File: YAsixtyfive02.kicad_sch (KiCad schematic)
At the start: 49 parts, among them J1 ~NMI, J2 Aux 5VDC, J3 Power 5V, J4 Expansion Bus, J5 Port A, J6 Port B, J7 GND, J8 FTDI Serial2USB, SW1 RESET, U1 WD65C02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

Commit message: changed PHI2 out to CLK and PCB tweaks
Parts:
- added JP4: ACIA CLK SEL, Connector_PinHeader_2.54mm:PinHeader_1x03_P2.54mm_Vertical, symbol Connector:Conn_01x03_Male
- U8: footprint 21-0248A -> Package_TO_SOT_THT:TO-92
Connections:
- net CLK: now also J4.20 (Pin_20), U4.5, U7.25 (PHI2), U9.14 (E/ϕ2), JP4.1 (Pin_1); no longer J4.36 (Pin_36), U9.3 (Rx_CLK), U9.4 (Tx_CLK)
- removed net PHI2: J4.20 (Pin_20), U1.39 (PHI2out), U4.5, U7.25 (PHI2), U9.14 (E/ϕ2)
- new net ACIA_CLK: J4.36 (Pin_36), JP4.3 (Pin_3)
- new net TX_CLK: JP4.2 (Pin_2), U9.3 (Rx_CLK), U9.4 (Tx_CLK)
- no-connect marks 13 -> 14

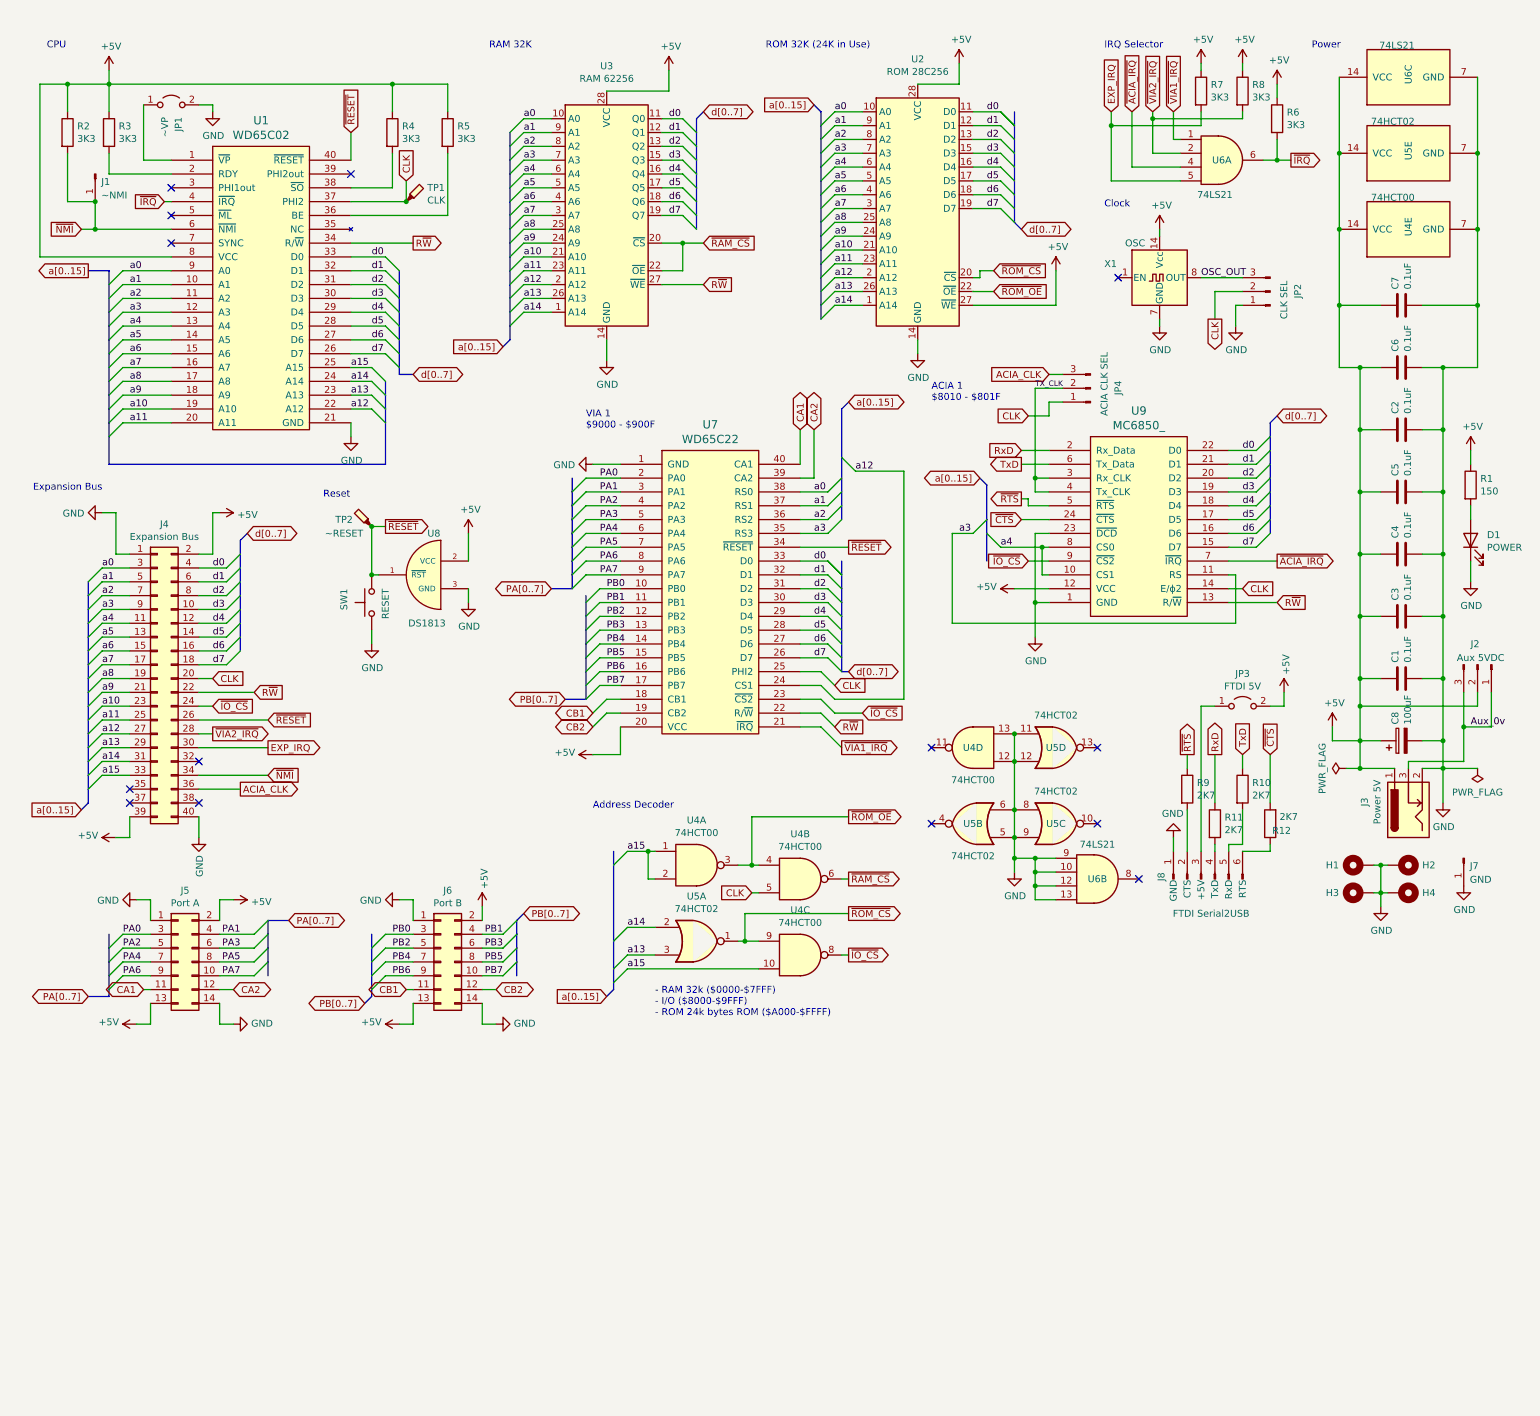
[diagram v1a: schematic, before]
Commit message: Simplified board for backplane  only CPU/RAM/ROM/ACIA/Glue
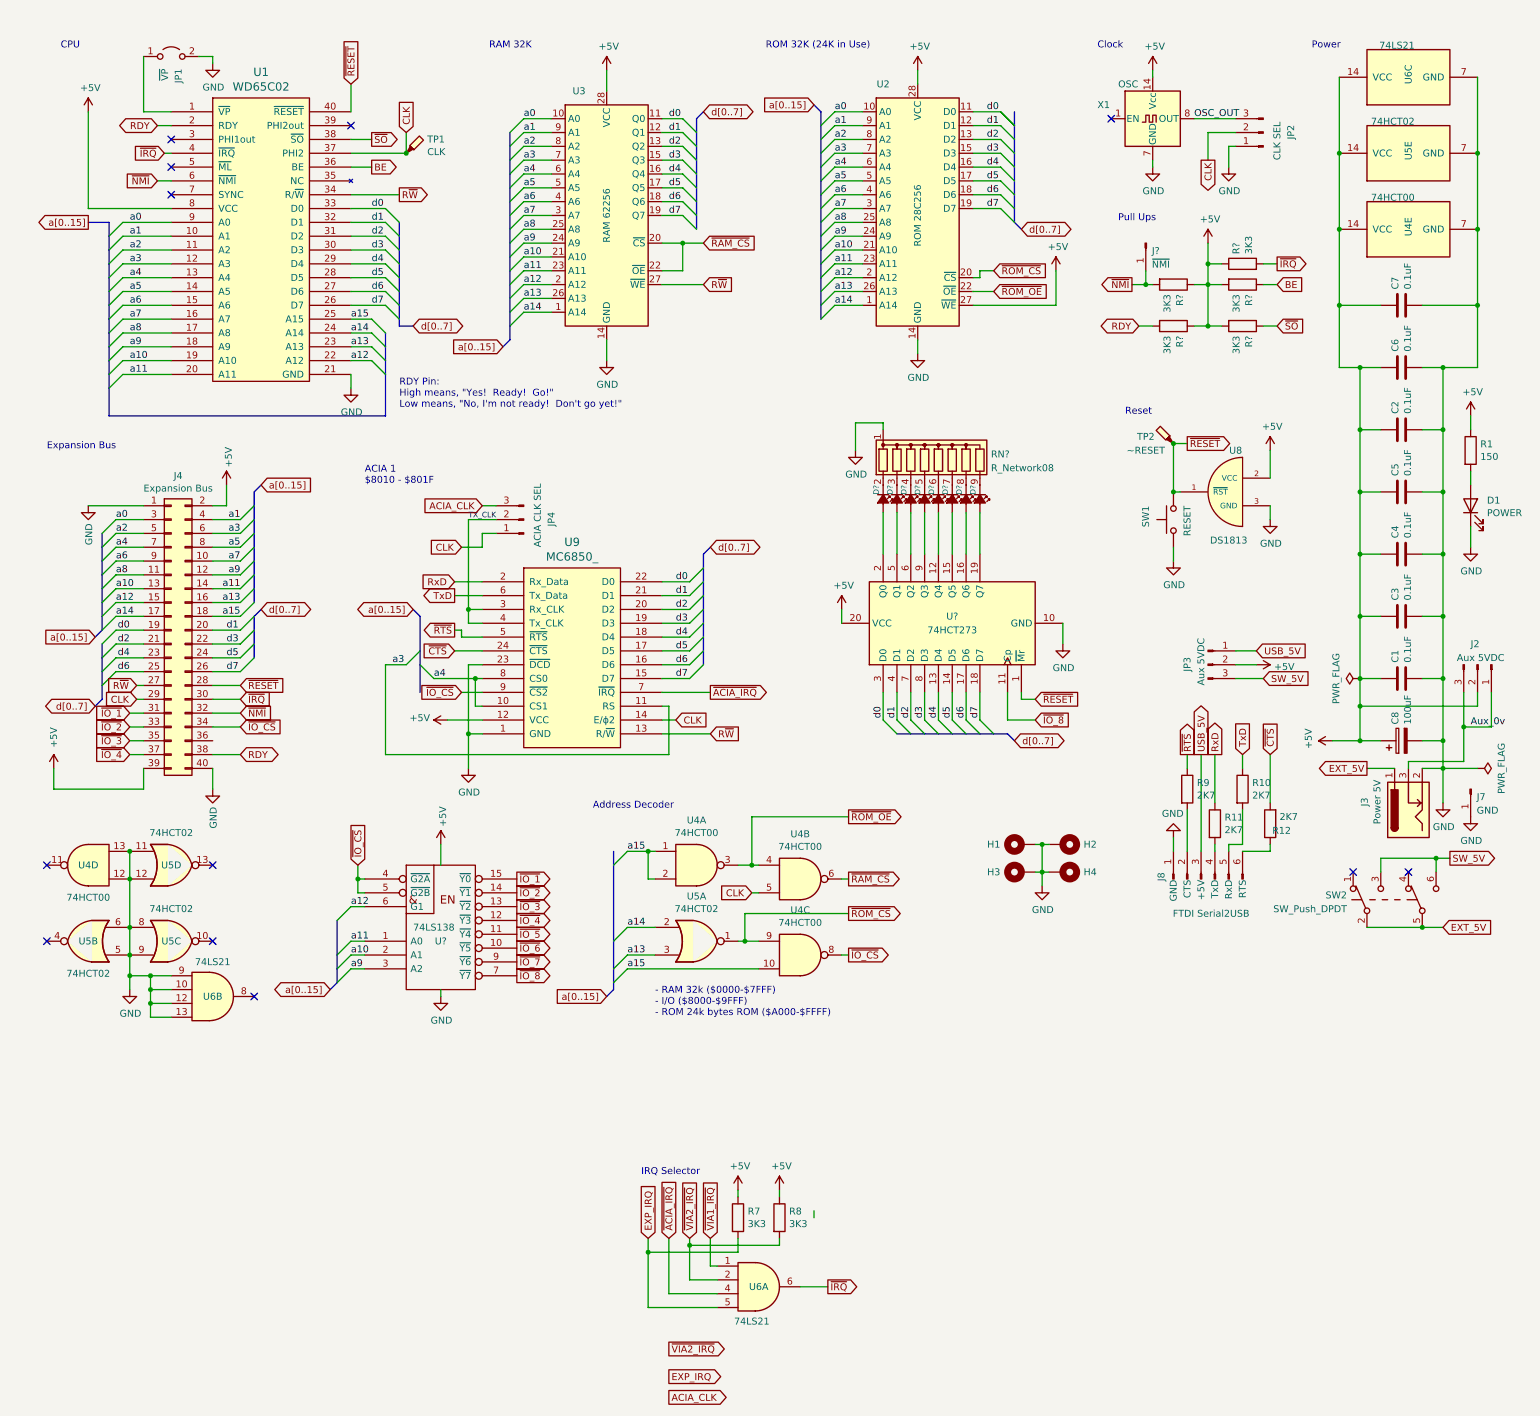
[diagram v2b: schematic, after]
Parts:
- removed J1: ~NMI, Connector_PinHeader_2.54mm:PinHeader_1x01_P2.54mm_Vertical, symbol Connector:Conn_01x01_Male
- removed J5: Port A, Connector_PinSocket_2.54mm:PinSocket_2x07_P2.54mm_Vertical, symbol Connector_Generic:Conn_02x07_Odd_Even
- removed J6: Port B, Connector_PinSocket_2.54mm:PinSocket_2x07_P2.54mm_Vertical, symbol Connector_Generic:Conn_02x07_Odd_Even
- removed JP3: FTDI 5V, Connector_PinHeader_2.54mm:PinHeader_2x01_P2.54mm_Vertical, symbol Jumper:Jumper_2_Open
- removed R2, R3, R4, R5, R6: 3K3, Resistor_THT:R_Axial_DIN0207_L6.3mm_D2.5mm_P10.16mm_Horizontal, symbol Device:R
- removed U7: WD65C22, Package_DIP:DIP-40_W15.24mm_Socket_LongPads, symbol 65xx:WD65C22
- added D?: CTL_0, symbol Device:LED_Small_Filled
- added D? (x5): 3, symbol Device:LED_Small_Filled
- added D?: CTL_1, symbol Device:LED_Small_Filled
- added D?: CTL_2, symbol Device:LED_Small_Filled
- added J?: ~{NMI}, Connector_PinHeader_2.54mm:PinHeader_1x01_P2.54mm_Vertical, symbol Connector:Conn_01x01_Male
- added JP3: Aux 5VDC, Connector_PinHeader_2.54mm:PinHeader_1x03_P2.54mm_Vertical, symbol Connector:Conn_01x03_Male
- added R? (x5): 3K3, Resistor_THT:R_Axial_DIN0207_L6.3mm_D2.5mm_P10.16mm_Horizontal, symbol Device:R
- added RN?: R_Network08, Resistor_THT:R_Array_SIP9, symbol Device:R_Network08
- added SW2: SW_Push_DPDT, Button_Switch_THT:SW_NKK_GW12LJP, symbol Switch:SW_Push_DPDT
- added U?: 74HCT273, symbol 74xx:74HCT273
- added U?: 74LS138, symbol 74xx_IEEE:74LS138
- JP1: value ~VP -> ~{VP}
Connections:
- net +5V: now also JP3.2 (Pin_2), R?.1, R?.1, R?.1, R?.2, R?.2, U?.16 (VCC), U?.20 (VCC); no longer J3.1
- net ACIA_CLK: no longer J4.36 (Pin_36)
- net CLK: now also J4.29 (Pin_29); no longer J4.20 (Pin_20)
- net EXP_IRQ: no longer J4.30 (Pin_30)
- net GND: now also RN?.1 (common), U?.10 (GND), U?.8 (GND)
- net R~{W}: now also J4.27 (Pin_27); no longer J4.22 (Pin_22)
- net a1: now also J4.4 (Pin_4); no longer J4.5 (Pin_5)
- net a10: now also J4.13 (Pin_13), U?.2 (A1); no longer J4.23 (Pin_23)
- net a11: now also J4.14 (Pin_14), U?.1 (A0); no longer J4.25 (Pin_25)
- net a12: now also J4.15 (Pin_15), U?.6 (G1); no longer J4.27 (Pin_27)
- net a13: now also J4.16 (Pin_16); no longer J4.29 (Pin_29)
- net a14: now also J4.17 (Pin_17); no longer J4.31 (Pin_31)
- net a15: now also J4.18 (Pin_18); no longer J4.33 (Pin_33)
- net a2: now also J4.5 (Pin_5); no longer J4.7 (Pin_7)
- net a3: now also J4.6 (Pin_6); no longer J4.9 (Pin_9)
- net a4: now also J4.7 (Pin_7); no longer J4.11 (Pin_11)
- net a5: now also J4.8 (Pin_8); no longer J4.13 (Pin_13)
- net a6: now also J4.9 (Pin_9); no longer J4.15 (Pin_15)
- net a7: now also J4.10 (Pin_10); no longer J4.17 (Pin_17)
- net a8: now also J4.11 (Pin_11); no longer J4.19 (Pin_19)
- net a9: now also J4.12 (Pin_12), U?.3 (A2); no longer J4.21 (Pin_21)
- net d0: now also J4.19 (Pin_19), U?.3 (D0); no longer J4.4 (Pin_4)
- net d1: now also J4.20 (Pin_20), U?.4 (D1); no longer J4.6 (Pin_6)
- net d2: now also J4.21 (Pin_21), U?.7 (D2); no longer J4.8 (Pin_8)
- net d3: now also J4.22 (Pin_22), U?.8 (D3); no longer J4.10 (Pin_10)
- net d4: now also J4.23 (Pin_23), U?.13 (D4); no longer J4.12 (Pin_12)
- net d5: now also J4.24 (Pin_24), U?.14 (D5); no longer J4.14 (Pin_14)
- net d6: now also J4.25 (Pin_25), U?.17 (D6); no longer J4.16 (Pin_16)
- net d7: now also J4.26 (Pin_26), U?.18 (D7); no longer J4.18 (Pin_18)
- net ~{IO_CS}: now also J4.34 (Pin_34), U?.4 (~{G2A}), U?.5 (~{G2B}); no longer J4.24 (Pin_24)
- net ~{IRQ}: now also J4.30 (Pin_30), R?.2
- net ~{NMI}: now also J4.32 (Pin_32), J?.1 (Pin_1), R?.2; no longer J4.34 (Pin_34)
- net ~{RESET}: now also J4.28 (Pin_28), U?.1 (~{Mr}); no longer J4.26 (Pin_26)
- net ~{VIA2_IRQ}: no longer J4.28 (Pin_28)
- net RDY: now reaches U1.2 (RDY)
- net RDY: now also J4.38 (Pin_38), R?.2
- net ~{SO}: now reaches U1.38 (~{SO})
- net ~{SO}: now also R?.1
- net BE: now reaches U1.36 (BE)
- net BE: now also R?.1
- net ~{IO_3}: now reaches J4.35 (Pin_35)
- net ~{IO_3}: now also U?.13 (~{Y2})
- net ~{IO_4}: now reaches J4.37 (Pin_37)
- net ~{IO_4}: now also U?.12 (~{Y3})
- net USB_5V: now reaches J8.3 (+5V)
- net USB_5V: now also JP3.1 (Pin_1)
- new net: D?.1 (K), RN?.2 (R1)
- new net: D?.2 (A), U?.2 (Q0)
- new net: D?.1 (K), RN?.6 (R5)
- new net: D?.2 (A), U?.12 (Q4)
- new net: D?.1 (K), RN?.3 (R2)
- new net: D?.2 (A), U?.5 (Q1)
- new net: D?.1 (K), RN?.4 (R3)
- new net: D?.2 (A), U?.6 (Q2)
- new net: D?.1 (K), RN?.8 (R7)
- new net: D?.2 (A), U?.16 (Q6)
- new net: D?.2 (A), U?.15 (Q5)
- new net: D?.2 (A), U?.19 (Q7)
- new net: D?.2 (A), U?.9 (Q3)
- new net: D?.1 (K), RN?.5 (R4)
- new net: D?.1 (K), RN?.7 (R6)
- new net: D?.1 (K), RN?.9 (R8)
- new net EXT_5V: J3.1, SW2.2 (B), SW2.5 (B)
- new net SW_5V: JP3.3 (Pin_3), SW2.3 (C), SW2.6 (C)
- new net ~{IO_1}: J4.31 (Pin_31), U?.15 (~{Y0})
- new net ~{IO_2}: J4.33 (Pin_33), U?.14 (~{Y1})
- new net ~{IO_5}: U?.11 (~{Y4})
- new net ~{IO_6}: U?.10 (~{Y5})
- new net ~{IO_7}: U?.9 (~{Y6})
- new net ~{IO_8}: U?.11 (Cp), U?.7 (~{Y7})
- no-connect marks 14 -> 12
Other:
- note added: "Pull Ups"
- note added: "RDY Pin: High means, "Yes! Ready! Go!" Low means, "No, I'm not ready! Don't go yet!""
- note removed: "VIA 1 $9000 - $900F"
- moved on the sheet: D1, H1, H2, H3, H4, J4, J7, JP1, JP2, JP4, R1, R7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

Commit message: Schematic annotated and ERC pass
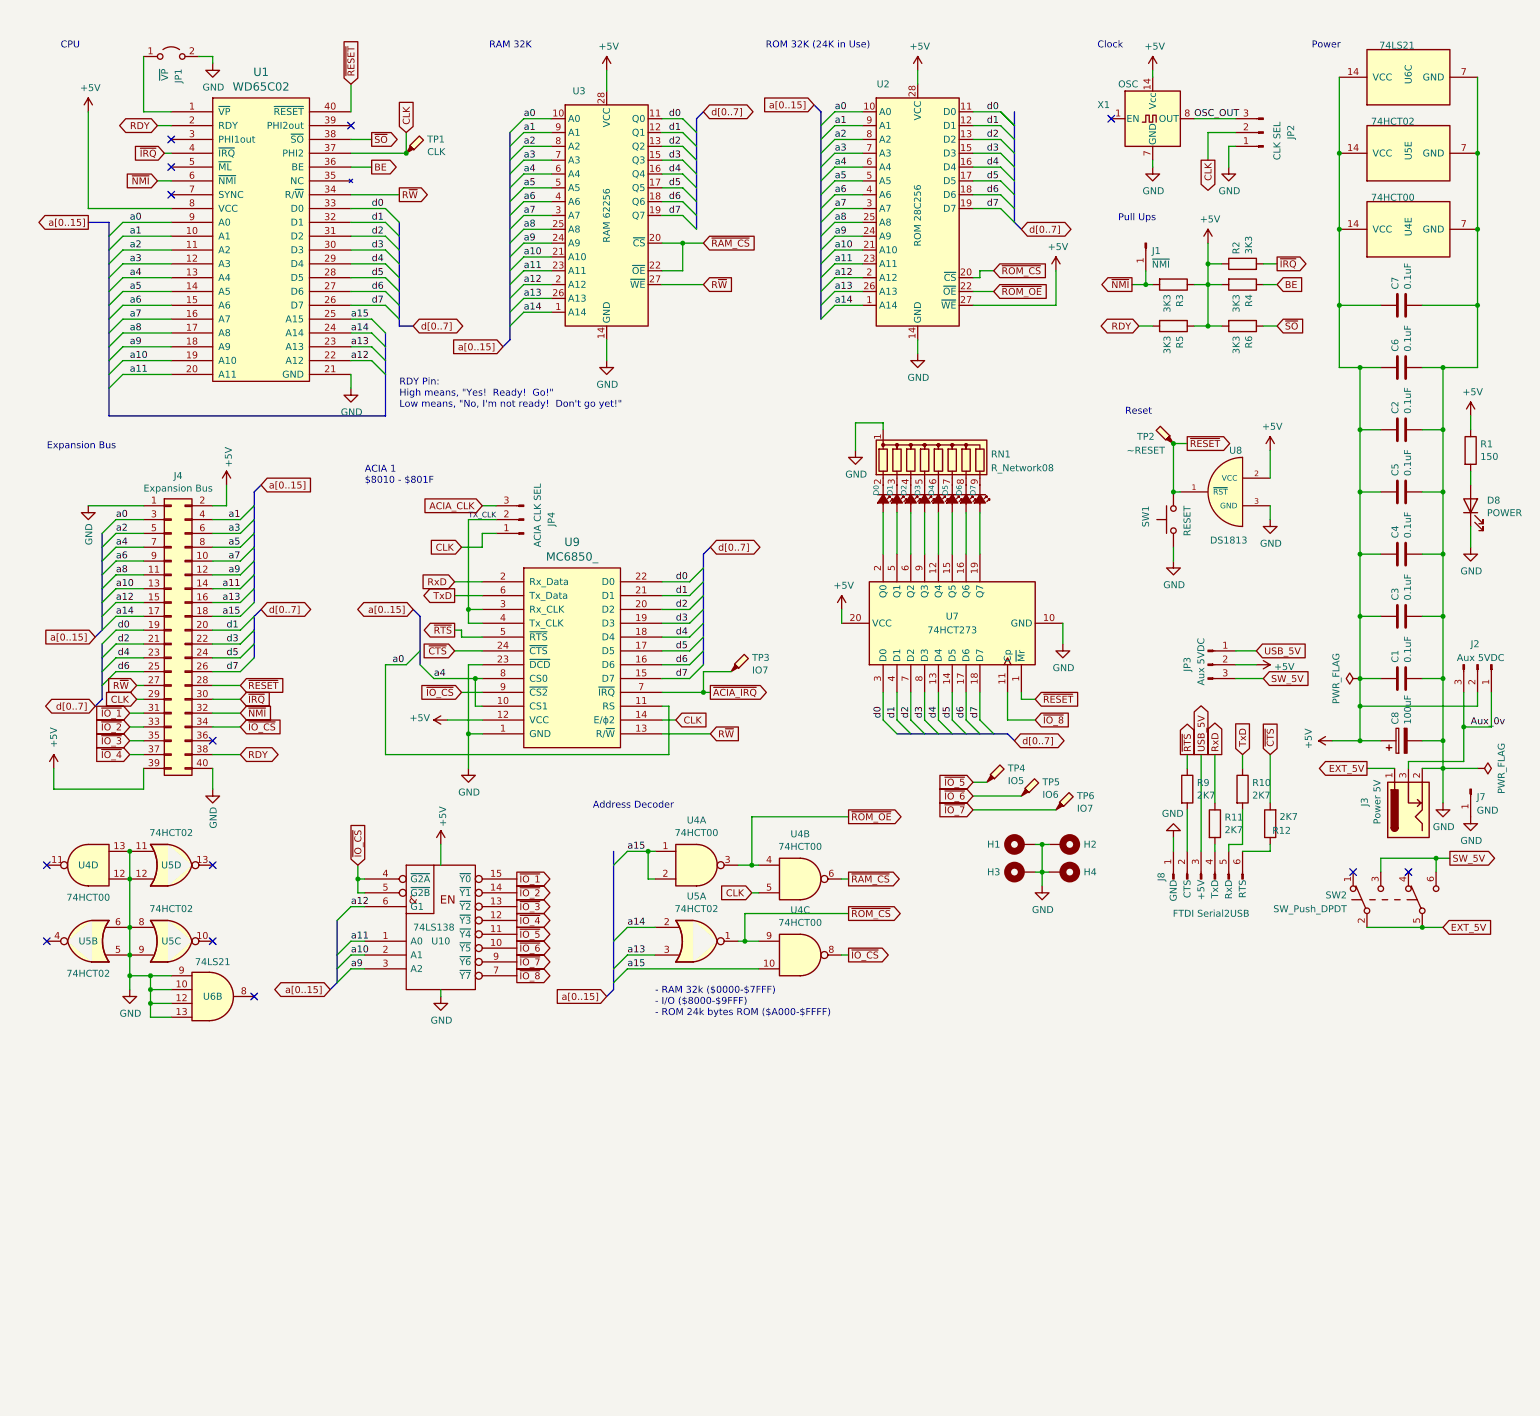
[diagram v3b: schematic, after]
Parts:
- removed R7, R8: 3K3, Resistor_THT:R_Axial_DIN0207_L6.3mm_D2.5mm_P10.16mm_Horizontal, symbol Device:R
- removed unit 1 of U6
- added TP3, TP6: IO7, TestPoint:TestPoint_THTPad_2.0x2.0mm_Drill1.0mm, symbol Connector:TestPoint_Probe
- added TP4: IO5, TestPoint:TestPoint_THTPad_2.0x2.0mm_Drill1.0mm, symbol Connector:TestPoint_Probe
- added TP5: IO6, TestPoint:TestPoint_THTPad_2.0x2.0mm_Drill1.0mm, symbol Connector:TestPoint_Probe
- D0, D1, D2, D3, D4, D5, D6, D7: renamed from D?; footprint (none) -> LED_THT:LED_D3.0mm
- U10: renamed from U?; footprint (none) -> Package_DIP:DIP-16_W7.62mm_LongPads
- U7: renamed from U?; footprint (none) -> Package_DIP:DIP-20_W7.62mm_Socket_LongPads
- gave numbers to parts that had none: 7
- renumbered D1 to D8
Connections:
- net a0: now also U9.11 (RS)
- net a3: no longer U9.11 (RS)
- net ~{ACIA_IRQ}: now also TP3.1
- net ~{IO_5}: now also TP4.1
- net ~{IO_6}: now also TP5.1
- net ~{IO_7}: now also TP6.1
- no-connect marks 12 -> 13
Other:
- note removed: "IRQ Selector"
